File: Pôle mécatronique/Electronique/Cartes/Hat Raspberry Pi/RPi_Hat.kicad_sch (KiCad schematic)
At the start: 11 parts, among them J1 Conn_02x03_Odd_Even, J3 Conn_01x02, U1 XBee, U2 MCP25625-x-SS, Y1 8MHz

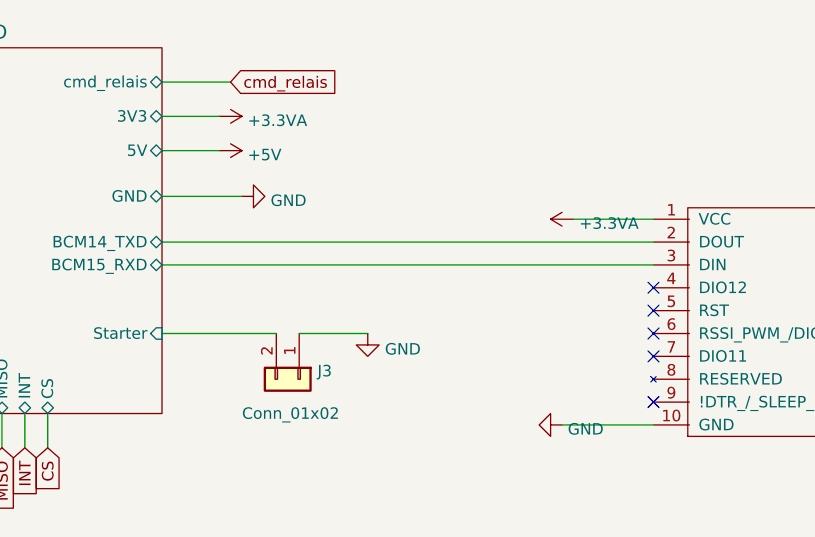
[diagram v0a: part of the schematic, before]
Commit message: Update BR
- Avancement raccords EN/MS1/MS2
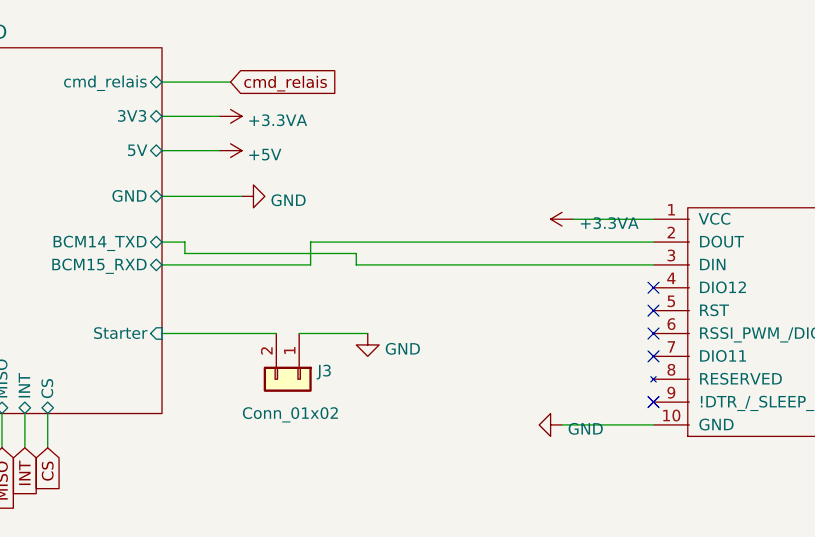
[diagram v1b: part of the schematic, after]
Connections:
- net RPi_GPIO/BCM14_TXD: now also U1.3 (DIN); no longer U1.2 (DOUT)
- net RPi_GPIO/BCM15_RXD: now also U1.2 (DOUT); no longer U1.3 (DIN)
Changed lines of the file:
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@@
+    (stroke (width 0) (type default) (color 0 0 0 0))
+  )
+  (wire (pts (xy 144.78 55.88) (xy 128.27 55.88))
     (stroke (width 0) (type default) (color 0 0 0 0))
   )
@@
     (stroke (width 0) (type default) (color 0 0 0 0))
   )
-  (wire (pts (xy 128.27 53.34) (xy 182.88 53.34))
-    (stroke (width 0) (type default) (color 0 0 0 0))
-  )
   (wire (pts (xy 133.35 115.57) (xy 143.51 115.57))
     (stroke (width 0) (type default) (color 0 0 0 0))
@@
   )
   (wire (pts (xy 100.33 153.67) (xy 102.87 153.67))
+    (stroke (width 0) (type default) (color 0 0 0 0))
+  )
+  (wire (pts (xy 182.88 53.34) (xy 144.78 53.34))
     (stroke (width 0) (type default) (color 0 0 0 0))
   )
@@
     (stroke (width 0) (type default) (color 0 0 0 0))
   )
-  (wire (pts (xy 128.27 55.88) (xy 182.88 55.88))
-    (stroke (width 0) (type default) (color 0 0 0 0))
-  )
   (wire (pts (xy 115.57 102.87) (xy 115.57 107.95))
     (stroke (width 0) (type default) (color 0 0 0 0))
@@
     (stroke (width 0) (type default) (color 0 0 0 0))
   )
+  (wire (pts (xy 149.86 54.61) (xy 130.81 54.61))
+    (stroke (width 0) (type default) (color 0 0 0 0))
+  )
   (wire (pts (xy 173.99 50.8) (xy 182.88 50.8))
     (stroke (width 0) (type default) (color 0 0 0 0))
   )
   (wire (pts (xy 135.89 123.19) (xy 135.89 128.27))
+    (stroke (width 0) (type default) (color 0 0 0 0))
+  )
+  (wire (pts (xy 149.86 55.88) (xy 149.86 54.61))
     (stroke (width 0) (type default) (color 0 0 0 0))
   )
@@
     (stroke (width 0) (type default) (color 0 0 0 0))
   )
+  (wire (pts (xy 182.88 55.88) (xy 149.86 55.88))
+    (stroke (width 0) (type default) (color 0 0 0 0))
+  )
   (wire (pts (xy 133.35 113.03) (xy 143.51 113.03))
     (stroke (width 0) (type default) (color 0 0 0 0))
@@
   )
   (wire (pts (xy 115.57 163.83) (xy 115.57 167.64))
+    (stroke (width 0) (type default) (color 0 0 0 0))
+  )
+  (wire (pts (xy 130.81 54.61) (xy 130.81 53.34))
     (stroke (width 0) (type default) (color 0 0 0 0))
   )
@@
   )
   (wire (pts (xy 209.55 121.92) (xy 209.55 125.73))
+    (stroke (width 0) (type default) (color 0 0 0 0))
+  )
+  (wire (pts (xy 128.27 53.34) (xy 130.81 53.34))
     (stroke (width 0) (type default) (color 0 0 0 0))
   )
@@
     (stroke (width 0) (type default) (color 0 0 0 0))
   )
+  (wire (pts (xy 144.78 53.34) (xy 144.78 55.88))
+    (stroke (width 0) (type default) (color 0 0 0 0))
+  )

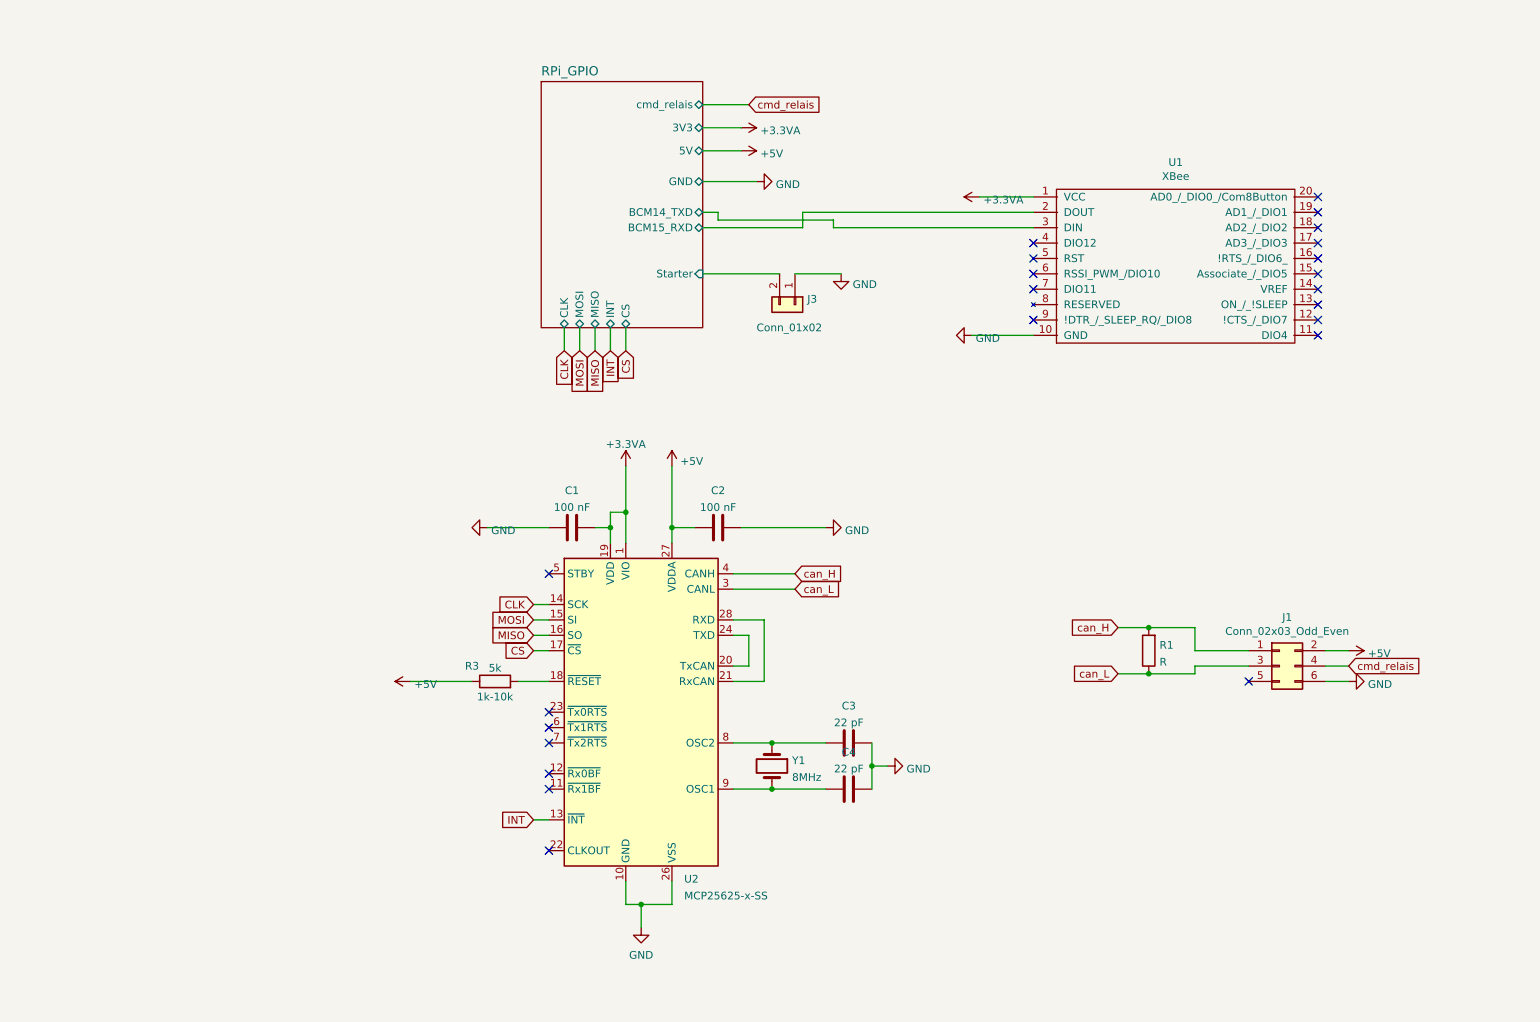
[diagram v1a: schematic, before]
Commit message: Udpate HAT
Sérigraphie
Points de tests
Arret d'urgence
I2C
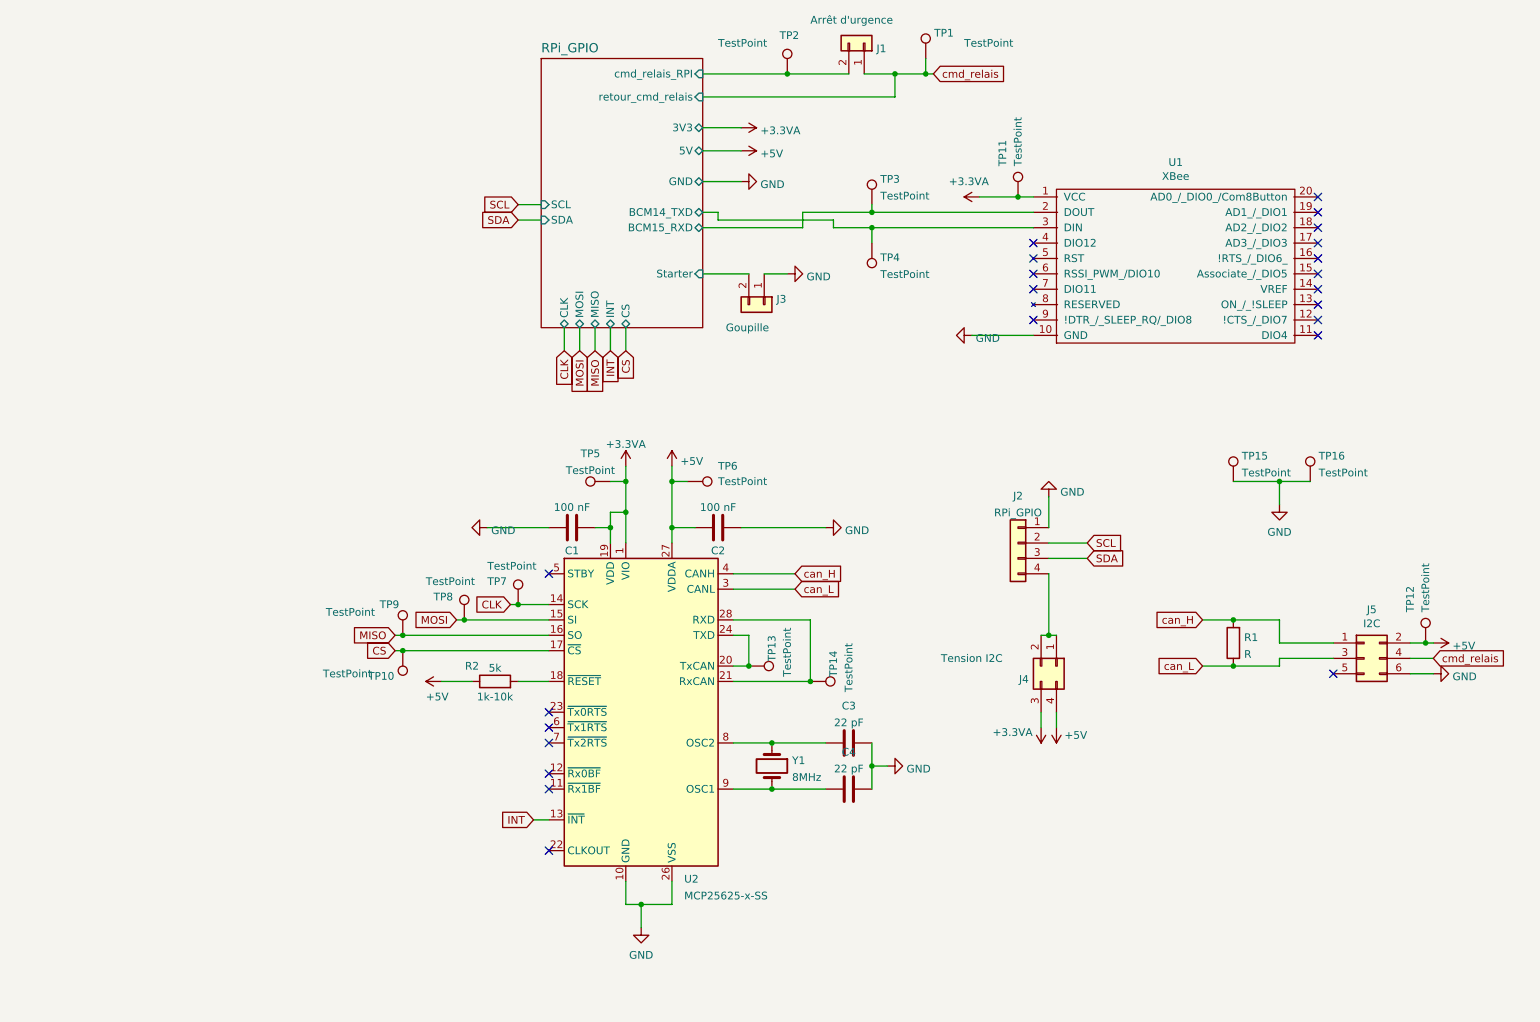
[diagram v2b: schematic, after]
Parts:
- added J1: Arrêt d'urgence, Connector_Hirose:Hirose_DF11-6DP-2DSA_2x03_P2.00mm_Vertical, symbol Connector_Generic:Conn_01x02
- added J2: RPi_GPIO, RPi_Hat:Pin_Header_Straight_2x20, symbol Connector_Generic:Conn_01x04
- added J4: Tension I2C, Connector_JST:JST_PH_B2B-PH-K_1x02_P2.00mm_Vertical, symbol Connector_Generic:Conn_02x02_Counter_Clockwise
- added TP1, TP10, TP11, TP12, TP13, TP14, TP2, TP3, TP4, TP5, TP6, TP7, TP8, TP9: TestPoint, TestPoint:TestPoint_Pad_D1.0mm, symbol Connector:TestPoint
- added TP15, TP16: TestPoint, TestPoint:TestPoint_Pad_D2.0mm, symbol Connector:TestPoint
- J3: value Conn_01x02 -> Goupille
- J5: renamed from J1; value Conn_02x03_Odd_Even -> I2C; footprint Connector_Hirose:Hirose_DF11-6DP-2DSA_2x03_P2.00mm_Vertical -> Connector_JST:JST_PH_B4B-PH-K_1x04_P2.00mm_Vertical
- Y1: footprint Crystal:Crystal_HC49-U_Vertical -> Crystal:Crystal_HC50_Horizontal
- renumbered R3 to R2
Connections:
- net +3.3VA: now also J4.3 (Pin_3), TP11.1, TP5.1
- net +5V: now also J4.4 (Pin_4), TP12.1, TP6.1
- net CLK: now also TP7.1
- net CS: now also TP10.1
- net GND: now also J2.1 (Pin_1), TP15.1, TP16.1
- net MISO: now also TP9.1
- net MOSI: now also TP8.1
- net RPi_GPIO/BCM14_TXD: now also TP4.1
- net RPi_GPIO/BCM15_RXD: now also TP3.1
- net cmd_relais: now also J1.1 (Pin_1), TP1.1
- net at U2.20 (TxCAN), U2.24 (TXD): now also TP13.1
- net at U2.21 (RxCAN), U2.28 (RXD): now also TP14.1
- new net: J2.4 (Pin_4), J4.1 (Pin_1), J4.2 (Pin_2)
- new net RPi_GPIO/cmd_relais_RPI: J1.2 (Pin_2), TP2.1
- new net SCL: J2.2 (Pin_2)
- new net SDA: J2.3 (Pin_3)
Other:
- sheet RPi_GPIO ports: added SCL, SDA, cmd_relais_RPI, retour_cmd_relais; removed cmd_relais
- moved on the sheet: J3, J5, R1

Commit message: Up random
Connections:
- net RPi_GPIO/BCM14_TXD renamed TDX
- net RPi_GPIO/BCM15_RXD renamed RDX
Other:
- moved on the sheet: C1, C2, C3, C4, J1, J3, R2, TP1, TP10, TP11, TP13, TP14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
